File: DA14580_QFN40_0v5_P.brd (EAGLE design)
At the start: 91 x 72 mm, 26 parts, among them CON1 CON_TC2030-CTL-NL, IC1 IC_SRAM_23K256_256K_32KBSN, IC2 74LVC1G00DBV, IC3 IC_LDO_XX1117, U1 IC_DA14580_QFN40, X1 SSW-114-02-S-S, X2 SSW-114-02-S-S

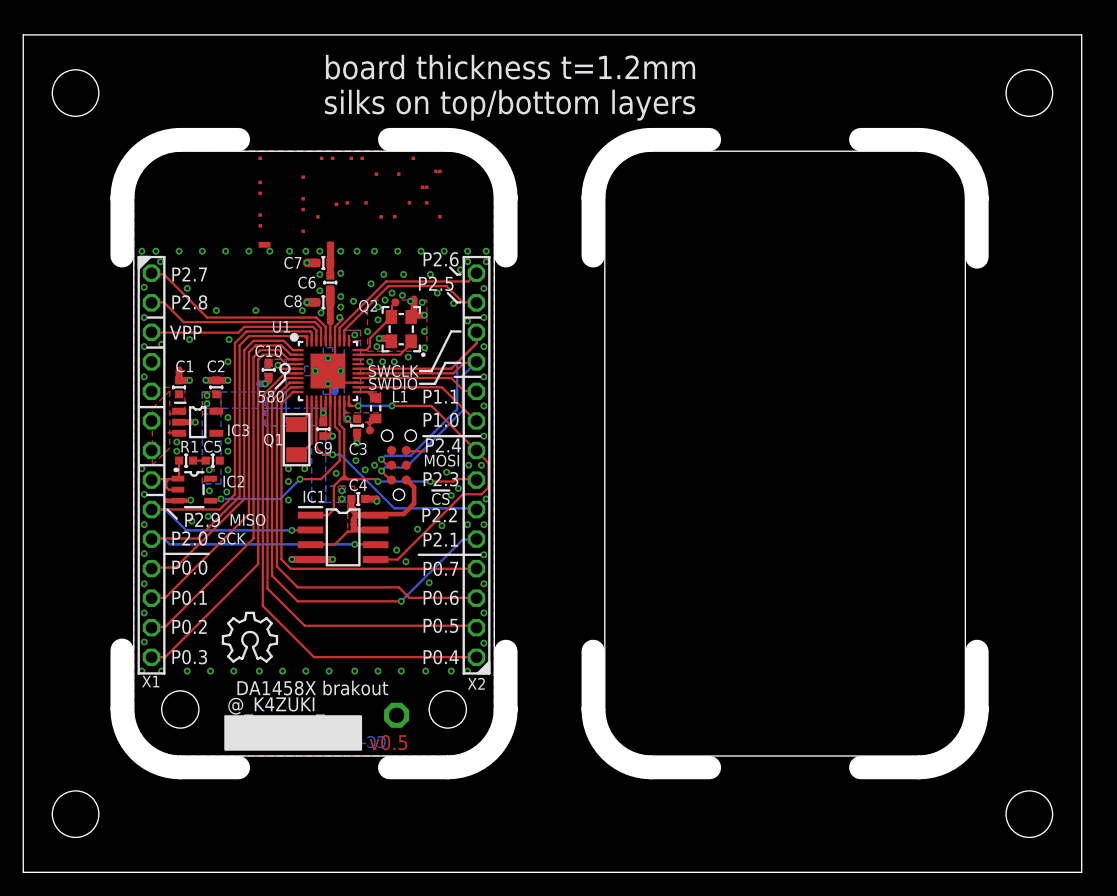
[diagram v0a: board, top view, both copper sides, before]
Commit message: [ FIX ][ 58X ] update schematic with library
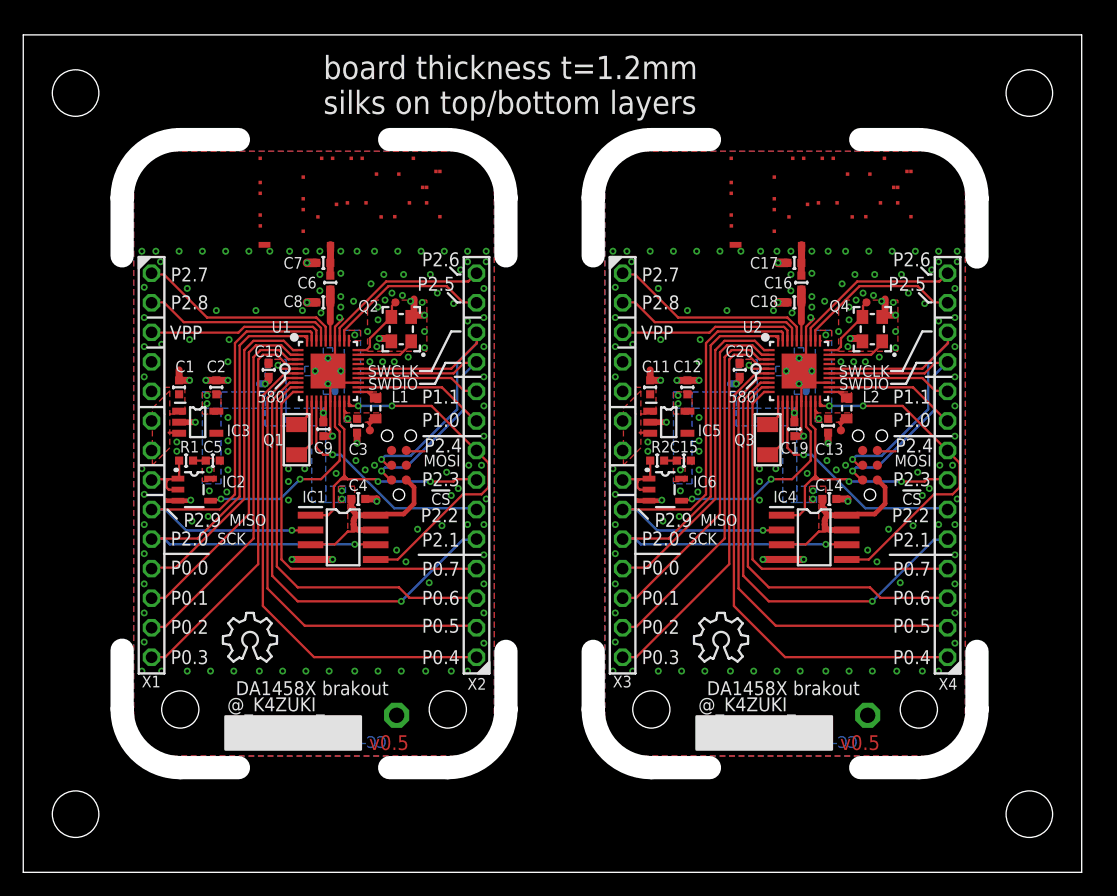
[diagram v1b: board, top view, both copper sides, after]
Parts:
- added C11, C12, C13, C14, C15, C16, C17, C18, C19, C20, R2: (no value), mylib:C0402
- added CON2: CON_TC2030-CTL-NL, mylib:CON_TC2030-IDC-NL
- added IC4: IC_MEMORY_8P_AT25XE011_SOP, mylib:IC_08_1.27_150MIL
- added IC5: IC_LDO_XX1117_5, mylib:IC_05_0.95_50MIL
- added IC6: 74LVC1G00DBV, 74xx-little-us_local:SOT23-5
- added L2: 2.2u, mylib:L_1608
- added Q3: (no value), mylib:CR_3216
- added Q4: (no value), mylib:CLOCK_2520
- added TP2, TP4: TPTP07R, testpad_local:TP07R
- added TP5: TPPAD1-13, testpad_local:P1-13
- added U$3: ANT_IFA, mylib:ANT_IFA_V2
- added U$4: ICON_OSHW, mylib:ICON_OSHW
- added U2: DA14583-AT2, mylib:QFN40_0.4P5.0X5.0
- added X3, X4: SSW-114-02-S-S, con-samtec.local:SSW-114-02-S-S
- IC1: value IC_SRAM_23K256_256K_32KBSN -> IC_MEMORY_8P_AT25XE011_SOP
- IC3: value IC_LDO_XX1117 -> IC_LDO_XX1117_5
- L1: value INDUCTOR_1608 -> 2.2u
- U1: value IC_DA14580_QFN40 -> DA14583-AT2
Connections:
- new net !RESET!1: IC6.1, IC6.2, R2.1, X3.8
- new net GND1: C11.2, C12.2, C13.2, C14.2, C15.2, C16.2, C17.1, C17.2, C18.2, C19.2, C20.2, CON2.5, IC4.4, IC5.2, IC6.3, Q4.2, Q4.4, TP5.TP, U$3.ANT, U$3.GND, U$3.GND@1, U$3.GND@10, U$3.GND@11, U$3.GND@12, U$3.GND@13, U$3.GND@14, U$3.GND@15, U$3.GND@16, U$3.GND@17, U$3.GND@18, U$3.GND@19, U$3.GND@2, U$3.GND@20, U$3.GND@21, U$3.GND@22, U$3.GND@23, U$3.GND@24, U$3.GND@25, U$3.GND@26, U$3.GND@27, U$3.GND@28, U$3.GND@29, U$3.GND@3, U$3.GND@30, U$3.GND@4, U$3.GND@5, U$3.GND@6, U$3.GND@7, U$3.GND@8, U$3.GND@9, U2.16, U2.23, U2.34, U2.BP, X3.4, X3.5
- new net N$10: C16.1, C18.1, U2.35
- new net N$2: Q3.1, U2.12
- new net N$3: Q3.2, U2.11
- new net N$4: Q4.1, U2.29
- new net N$5: Q4.3, TP4.TP, U2.30
- new net N$7: L2.2, U2.21
- new net N$8: C13.1, L2.1, TP2.TP, U2.19, U2.31
- new net P0_10: U2.3, X3.13
- new net P0_11: U2.4, X3.14
- new net P0_12: U2.7, X4.2
- new net P0_13: U2.6, X4.1
- new net P0_14: U2.10, X4.4
- new net P0_15: U2.9, X4.3
- new net P0_8: U2.1, X3.11
- new net P0_9: U2.2, X3.12
- new net P1_4: U2.22, X4.9
- new net P1_5: U2.24, X4.10
- new net P1_6: U2.27
- new net P1_7: U2.28
- new net P2_10: IC4.1, U2.18, X4.7
- new net P2_11: U2.13, X4.6
- new net P2_12: IC4.6, U2.40, X3.10
- new net P2_13: U2.8, X4.5
- new net P2_14: U2.32, X4.13
- new net P2_15: U2.33, X4.14
- new net P2_16: IC4.2, U2.39, X3.9
- new net P2_17: IC4.5, U2.20, X4.8
- new net P2_18: U2.36, X3.1
- new net P2_19: U2.37, X3.2
- new net RESET1: IC6.4, U2.17
- new net SWCLK1: CON2.4, U2.26, X4.12
- new net SWDIO1: CON2.2, U2.25, X4.11
- new net VCC1: C12.1, C14.1, C15.1, C19.1, C20.1, CON2.1, IC4.3, IC4.7, IC4.8, IC5.5, IC6.5, R2.2, U2.14, U2.15, U2.5
- new net VDD1: C11.1, IC5.1, IC5.3, X3.6, X3.7
- new net VPP1: U2.38, X3.3
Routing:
- net P2_12: track 0.00 -> 48.4 mm, vias 0 -> 1
- net P2_16: track 0.00 -> 42.9 mm, vias 0 -> 1
- net P0_13: track 0.00 -> 42.1 mm
- net GND1: track 0.00 -> 41.7 mm, vias 0 -> 148
- net P0_12: track 0.00 -> 39.1 mm
- net P2_13: track 0.00 -> 38.6 mm, vias 0 -> 1
- net P0_15: track 0.00 -> 34.8 mm
- net P0_11: track 0.00 -> 34.0 mm
- net P0_14: track 0.00 -> 32.3 mm
- net P0_10: track 0.00 -> 31.9 mm
- net P0_9: track 0.00 -> 30.0 mm
- net P2_17: track 0.00 -> 29.2 mm, vias 0 -> 2
- net SWCLK1: track 0.00 -> 28.9 mm, vias 0 -> 1
- net P0_8: track 0.00 -> 28.5 mm
- net SWDIO1: track 0.00 -> 25.6 mm, vias 0 -> 1
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- added copper zone on layer 1, net GND1
- added copper zone on layer 16, net GND1
- added copper zone on layer 1, net N$7
- added copper zone on layer 1, net N$8
- added copper zone on layer 16, net N$8
- added copper zone on layer 1, net VCC1
- added copper zone on layer 16, net VCC1
- added copper zone on layer 1, net VDD1
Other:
- outline, holes or cut-outs redrawn
- board text added: "C1"
- board text added: "C10"
- board text added: "C2"
- board text added: "C3"
- board text added: "C4"
- board text added: "C5"
- board text added: "C6"
- board text added: "C7"
- board text added: "C8"
- board text added: "C9"
- board text added: "IC1"
- board text added: "IC2"
- board text added: "IC3"
- board text added: "L1"
- board text added: "Q1"
- board text added: "Q2"
- board text added: "R1"
- board text added: "U1"
- board text added: "X1"
- board text added: "X2"

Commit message: [ 58x ] panelize and process gerber
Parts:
- added TP7, TP8: TPTP07R, testpad_local:TP07R
- added TP9: TPPAD1-13, testpad_local:P1-13
- C16, C6: value (none) -> NM
- IC1, IC4: value IC_MEMORY_8P_AT25XE011_SOP -> 1265-1137-1-ND
- IC2, IC6: value 74LVC1G00DBV -> NC7SZ00M5XCT-ND
- L1, L2: value 2.2u -> (none)
- Q1, Q3: value (none) -> 728-1076-1-ND; device mylib:CR_3216 -> mylib:CRYSTAL_FC-135
- Q2, Q4: value (none) -> 887-1833-1-ND
- TP2, TP4: value TPTP07R -> TESTPAD_F; device testpad_local:TP07R -> mylib:FIDUCIAL
- TP5: value TPPAD1-13 -> TESTPAD_F; device testpad_local:P1-13 -> mylib:FIDUCIAL
- moved TP4 72.4 mm to (15.0, 5.00)
- moved TP2 62.9 mm to (15.0, 68.0)
- moved TP5 8.52 mm to (72.0, 5.00)
- moved C11 1.00 mm to (54.9, 41.7)
- moved C12 1.00 mm to (58.1, 41.7)
- moved C13 1.00 mm to (70.2, 38.4)
- moved C14 1.00 mm to (70.3, 32.1)
- moved C15 1.00 mm to (57.8, 35.4)
- moved C16 1.00 mm to (67.9, 50.7)
- moved C17 1.00 mm to (67.3, 52.4)
- moved C18 1.00 mm to (67.3, 49.0)
- moved C19 1.00 mm to (67.3, 38.1)
- moved C20 1.00 mm to (62.6, 43.2)
- moved CON2 1.00 mm to (73.8, 35.0)
- moved IC4 1.00 mm to (69.0, 28.8)
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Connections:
- net GND1: now also TP9.TP; no longer TP5.TP
- net N$5: now also TP8.TP; no longer TP4.TP
- net N$8: now also TP7.TP; no longer TP2.TP
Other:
- board size 91 x 72 mm -> 92 x 73 mm

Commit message: [58x] Gerber out; BOM update
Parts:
- removed TP7, TP8: TPTP07R, testpad_local:TP07R
- removed TP9: TPPAD1-13, testpad_local:P1-13
- added TP91, TP92, TP93: TESTPAD_F, mylib:FIDUCIAL
- C17, C18, C7, C8: value (none) -> NM
- IC1, IC4: value 1265-1137-1-ND -> IC_MEMORY_8P_AT25XE011_SOP
- IC3, IC5: value IC_LDO_XX1117_5 -> LDO5_3.3_SOT23
- Q1, Q3: value 728-1076-1-ND -> 32.768k
- Q2, Q4: value 887-1833-1-ND -> 16M/2520
- TP1: value TPTP07R -> TESTPAD; device testpad_local:TP07R -> mylib:TP06RECT
- TP2, TP5: value TESTPAD_F -> TESTPAD; device mylib:FIDUCIAL -> mylib:TP06RECT
- TP3: value TPTP07R -> TPPAD1-13; device testpad_local:TP07R -> testpad_local:P1-13
- TP4: value TESTPAD_F -> TPPAD1-13; device mylib:FIDUCIAL -> testpad_local:P1-13
- TP6: value TPPAD1-13 -> TESTPAD; device testpad_local:P1-13 -> mylib:TP06RECT
- U1, U2: value DA14583-AT2 -> DA14583AT2
- moved TP4 59.2 mm to (73.6, 13.5)
- moved TP6 54.2 mm to (73.5, 49.0), turned to 90 degrees
- moved TP3 35.5 mm to (32.6, 13.5)
- moved TP5 32.9 mm to (71.3, 37.9)
- moved TP2 25.8 mm to (32.5, 49.0), turned to 90 degrees
- moved TP1 0.10 mm to (30.3, 37.9)
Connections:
- net GND: now also TP3.TP; no longer TP6.TP
- net GND1: now also TP4.TP; no longer TP9.TP
- net N$21: now also TP2.TP; no longer TP3.TP
- net N$5: now also TP6.TP; no longer TP8.TP
- net N$8: now also TP5.TP; no longer TP7.TP
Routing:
- net VCC1: track 23.3 -> 24.7 mm
- net VCC: track 23.3 -> 24.7 mm
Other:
- board text added: "DA14583-AT2 DA14580-AT2"
- board text removed: "01-16"
- board text removed: "01-20"
- board text removed: "LAYER-STACK"
